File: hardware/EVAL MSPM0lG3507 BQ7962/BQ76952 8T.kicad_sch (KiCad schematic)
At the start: 54 parts, among them U11 FCX495, U13 PBQ76952PFBT, U14 FCX495

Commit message: kjcaejjacljace
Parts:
- added D3: D_Schottky_Small, symbol Device:D_Schottky_Small
- added R45: 200, Resistor_SMD:R_1206_3216Metric_Pad1.30x1.75mm_HandSolder, symbol Device:R_US
- added TP18: TestPoint, TestPoint:TestPoint_Loop_D2.50mm_Drill1.0mm_LowProfile, symbol Connector:TestPoint
- C36, C37, C38, C42, C43, C44, C45, C46, C47, C48, C49, C50, C51, C52, C53, C54, C55: mouser (none) -> https://www.mouser.com/ProductDetail/Samsung-Electro-Mechan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; specs (none) -> 50VDC, X7R, 10%, -55C, +125C, 220nF; unit x10 (none) -> 0.05
- C57: specs (none) -> 10uF, 50VDC, X5R, 10%, -55C, +85C; unit x10 (none) -> 0.07
- R72: mouser (none) -> https://www.mouser.com/ProductDetail/Panasonic/ERJ-P08J201V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; specs (none) -> 200Ohms, 660mW, 200PPM, 500V, 5%, -55C, +155C
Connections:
- net 16P: now also R45.2; no longer R65.2, U11.2
- net BAT: now also TP18.1
- new net: R45.1, R65.2, U11.2
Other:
- note added: "raise to 3.3v to shut off device"
- moved on the sheet: TP8

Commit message: mouser doom scrolling labor
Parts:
- removed C62: 1u, Capacitor_SMD:C_1812_4532Metric, symbol Device:C_Small
- removed D3: D_Schottky_Small, symbol Device:D_Schottky_Small
- removed R65: 50k, Resistor_SMD:R_1206_3216Metric_Pad1.30x1.75mm_HandSolder, symbol Device:R_US
- added C1, C2, C4, C6, C7: 10u, Capacitor_SMD:C_1206_3216Metric_Pad1.33x1.80mm_HandSolder, symbol Device:C_Small
- added D3: 36V, symbol Device:D_Zener_Small
- added R27, R46: 100k, Resistor_SMD:R_1206_3216Metric_Pad1.30x1.75mm_HandSolder, symbol Device:R_US
- C30, C56, C58, C59, C60, C61: mouser (none) -> https://www.mouser.com/ProductDetail/Walsin/1206B104K251CT?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; specs (none) -> 100nF, 250VDC, X7R, 10%, -55C, +125C; unit x10 (none) -> 0.062
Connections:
- net BAT: now also C1.1, C2.1, C4.1, C6.1
- net Series Sense N: now also C1.2, C2.2, C4.2, C6.2, C7.2, D3.2 (A)
- net at C56.1, U11.1: now also D3.1 (K), R46.1
- net at R45.1, U11.2: now also R27.2
- net at R72.2, U14.2: now also C7.1
- new net: R27.1, R46.2
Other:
- note added: "buffer caps. 434ms op @ 300mA from 6v src"
- note added: "power supply input pin (50V abs max, limited by caps)"
- moved on the sheet: C56

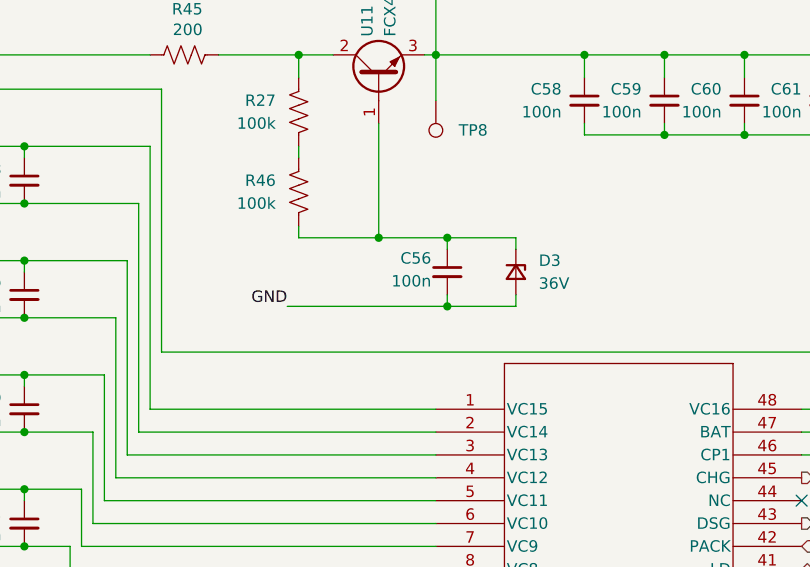
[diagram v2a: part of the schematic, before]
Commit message: ti once again making the most convenient IC's around
new TVS solution. use the
TPD4E05U06DQA
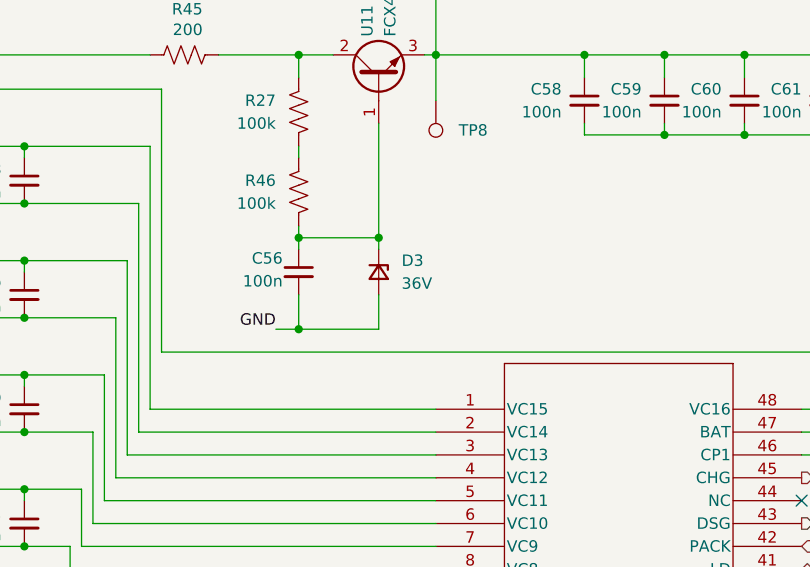
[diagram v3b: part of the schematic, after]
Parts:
- U11, U14: unit x10 (none) -> 0.34
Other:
- moved on the sheet: C56, D3
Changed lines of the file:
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@@
 	)
 	(junction
-		(at 135.89 54.61)
-		(diameter 0)
-		(color 0 0 0 0)
-	)
-	(junction
 		(at 176.53 43.18)
 		(diameter 0)
@@
 	)
 	(junction
+		(at 135.89 54.61)
+		(diameter 0)
+		(color 0 0 0 0)
+	)
+	(junction
 		(at 90.17 44.45)
 		(diameter 0)
@@
 	)
 	(junction
-		(at 90.17 95.25)
+		(at 127 64.77)
 		(diameter 0)
 		(color 0 0 0 0)
 	)
 	(junction
-		(at 143.51 62.23)
+		(at 90.17 95.25)
 		(diameter 0)
 		(color 0 0 0 0)
@@
 	)
 	(junction
+		(at 127 54.61)
+		(diameter 0)
+		(color 0 0 0 0)
+	)
+	(junction
 		(at 96.52 44.45)
 		(diameter 0)
@@
 	)
 	(junction
-		(at 143.51 54.61)
-		(diameter 0)
-		(color 0 0 0 0)
-	)
-	(junction
 		(at 190.5 52.07)
 		(diameter 0)
@@
 	(wire
 		(pts
-			(xy 143.51 60.96) (xy 143.51 62.23)
-		)
-		(stroke
-			(width 0)
-			(type default)
-		)
-	)
-	(wire
-		(pts
 			(xy 53.34 44.45) (xy 72.39 44.45)
 		)
@@
 	(wire
 		(pts
-			(xy 135.89 54.61) (xy 143.51 54.61)
-		)
-		(stroke
-			(width 0)
-			(type default)
-		)
-	)
-	(wire
-		(pts
 			(xy 90.17 57.15) (xy 96.52 57.15)
 		)
@@
 	(wire
 		(pts
+			(xy 127 60.96) (xy 127 64.77)
+		)
+		(stroke
+			(width 0)
+			(type default)
+		)
+	)
+	(wire
+		(pts
 			(xy 90.17 107.95) (xy 96.52 107.95)
 		)
@@
 	(wire
 		(pts
+			(xy 127 54.61) (xy 135.89 54.61)
+		)
+		(stroke
+			(width 0)
+			(type default)
+		)
+	)
+	(wire
+		(pts
 			(xy 90.17 128.27) (xy 90.17 127)
 		)
@@
 	(wire
 		(pts
-			(xy 151.13 62.23) (xy 151.13 60.96)
+			(xy 135.89 64.77) (xy 135.89 60.96)
 		)
 		(stroke
@@
 	(wire
 		(pts
-			(xy 151.13 62.23) (xy 143.51 62.23)
+			(xy 135.89 64.77) (xy 127 64.77)
 		)
 		(stroke
@@
 	(wire
 		(pts
-			(xy 127 54.61) (xy 135.89 54.61)
-		)
-		(stroke
-			(width 0)
-			(type default)
-		)
-	)
-	(wire
-		(pts
 			(xy 138.43 132.08) (xy 138.43 134.62)
 		)
@@
 	(wire
 		(pts
-			(xy 143.51 55.88) (xy 143.51 54.61)
+			(xy 127 55.88) (xy 127 54.61)
 		)
 		(stroke
@@
 	(wire
 		(pts
-			(xy 151.13 54.61) (xy 143.51 54.61)
-		)
-		(stroke
-			(width 0)
-			(type default)
-		)
-	)
-	(wire
-		(pts
 			(xy 46.99 72.39) (xy 52.07 72.39)
 		)
@@
 	(wire
 		(pts
-			(xy 151.13 54.61) (xy 151.13 55.88)
+			(xy 135.89 54.61) (xy 135.89 55.88)
 		)
 		(stroke
@@
 	(wire
 		(pts
-			(xy 125.73 62.23) (xy 143.51 62.23)
+			(xy 124.46 64.77) (xy 127 64.77)
 		)
 		(stroke
@@
 	)
 	(label "GND"
-		(at 125.73 62.23 180)
+		(at 124.46 64.77 180)
 		(effects
 			(font
@@
 			)
 		)
+		(property "unit x10" "0.34"
+			(at 135.89 35.56 0)
+			(effects
+				(font
+					(size 1.27 1.27)
+				)
+				(hide yes)
+			)
+		)
 		(pin "1"
 		)
@@
 	)
 	(symbol
-		(lib_name "FCX485_NPN_BJT_1")
 		(lib_id "zzLocalLibrary:FCX485_NPN_BJT")
 		(at 207.01 95.25 0)
@@
 			)
 		)
+		(property "unit x10" "0.34"
+			(at 207.01 95.25 0)
+			(effects
+				(font
+					(size 1.27 1.27)
+				)
+				(hide yes)
+			)
+		)
 		(pin "1"
 		)
@@
 	(symbol
 		(lib_id "Device:C_Small")
-		(at 143.51 58.42 0)
+		(at 127 58.42 0)
 		(mirror y)
 		(unit 1)
@@
 		(dnp no)
 		(property "Reference" "C56"
-			(at 141.732 56.896 0)
+			(at 125.222 56.896 0)
 			(effects
 				(font
@@
 		)
 		(property "Value" "100n"
-			(at 141.732 59.436 0)
+			(at 125.222 59.436 0)
 			(effects
 				(font
@@
 		)
 		(property "Footprint" "Capacitor_SMD:C_1206_3216Metric_Pad1.33x1.80mm_HandSolder"
-			(at 143.51 58.42 0)
+			(at 127 58.42 0)
 			(effects
 				(font
@@
 		)
 		(property "Datasheet" ""
-			(at 143.51 58.42 0)
+			(at 127 58.42 0)
 			(effects
 				(font
@@
 		)
 		(property "Description" ""
-			(at 143.51 58.42 0)
+			(at 127 58.42 0)
 			(effects
 				(font
@@
 		)
 		(property "Sim.Device" ""
-			(at 143.51 58.42 0)
+			(at 127 58.42 0)
 			(effects
 				(font
@@
 		)
 		(property "Sim.Type" ""
-			(at 143.51 58.42 0)
+			(at 127 58.42 0)
 			(effects
 				(font
@@
 		)
 		(property "mouser" "https://www.mouser.com/ProductDetail/Walsin/1206B104K251CT?qs=fIkAfuXiAQKkmX5niKUTKw%3D%3D"
-			(at 143.51 58.42 0)
+			(at 127 58.42 0)
 			(effects
 				(font
@@
 		)
 		(property "specs" "100nF, 250VDC, X7R, 10%, -55C, +125C"
-			(at 143.51 58.42 0)
+			(at 127 58.42 0)
 			(effects
 				(font
@@
 		)
 		(property "unit x10" "0.062"
-			(at 143.51 58.42 0)
+			(at 127 58.42 0)
 			(effects
 				(font
@@
 	(symbol
 		(lib_id "Device:D_Zener_Small")
-		(at 151.13 58.42 270)
+		(at 135.89 58.42 270)
 		(unit 1)
 		(exclude_from_sim no)
@@
 		(fields_autoplaced yes)
 		(property "Reference" "D3"
-			(at 153.67 57.1499 90)
+			(at 138.43 57.1499 90)
 			(effects
 				(font
@@
 		)
 		(property "Value" "36V"
-			(at 153.67 59.6899 90)
+			(at 138.43 59.6899 90)
 			(effects
 				(font
@@
 		)
 		(property "Footprint" ""
-			(at 151.13 58.42 90)
+			(at 135.89 58.42 90)
 			(effects
 				(font
@@
 		)
 		(property "Datasheet" "~"
-			(at 151.13 58.42 90)
+			(at 135.89 58.42 90)
 			(effects
 				(font
@@
 		)
 		(property "Description" "Zener diode, small symbol"
-			(at 151.13 58.42 0)
+			(at 135.89 58.42 0)
 			(effects
 				(font
@@
 		)
 		(property "mouser" "https://www.mouser.com/ProductDetail/Vishay/MMSZ4715-HE3_A-08?qs=Imq1NPwxi74N8IHyuuRB%252BQ%3D%3D"
-			(at 151.13 58.42 0)
+			(at 135.89 58.42 0)
 			(effects
 				(font
@@
 		)
 		(property "specs" "36V, 500mW, 5%, 1nA, -55C, +150C"
-			(at 151.13 58.42 0)
+			(at 135.89 58.42 0)
 			(effects
 				(font
@@
 		)
 		(property "unit x10" "0.27"
-			(at 151.13 58.42 0)
+			(at 135.89 58.42 0)
 			(effects
 				(font

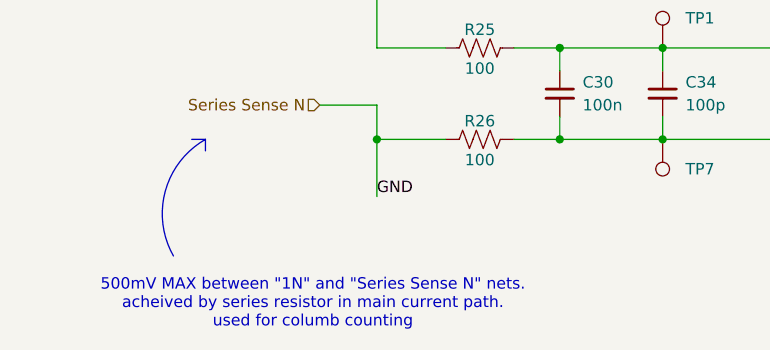
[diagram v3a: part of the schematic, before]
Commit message: corrected mosfet choice and started jumper board with xds110
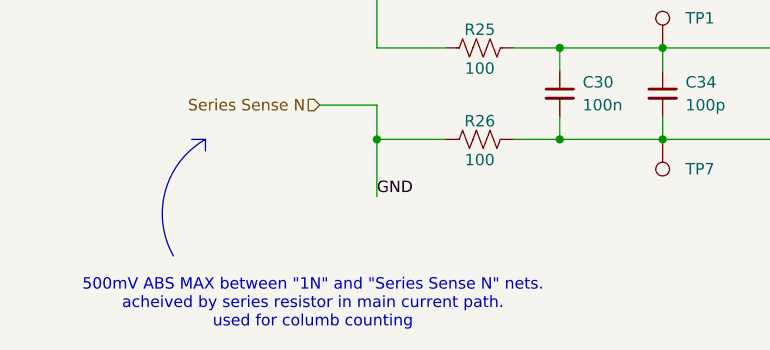
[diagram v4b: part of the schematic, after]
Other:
- note added: "500mV ABS MAX between "1N" and "Series Sense N" nets. acheived by series resistor in main current path. used for columb counting"
- note removed: "500mV MAX between "1N" and "Series Sense N" nets. acheived by series resistor in main current path. used for columb counting"
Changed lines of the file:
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@@
 		)
 	)
-	(text "500mV MAX between \"1N\" and \"Series Sense N\" nets.\nacheived by series resistor in main current path.\nused for columb counting"
+	(text "500mV ABS MAX between \"1N\" and \"Series Sense N\" nets.\nacheived by series resistor in main current path.\nused for columb counting"
 		(exclude_from_sim no)
 		(at 46.228 191.008 0)

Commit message: indicated layout so someone else can do it
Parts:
- D3: footprint (none) -> Diode_SMD:D_SOD-123
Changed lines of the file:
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@@
 			)
 		)
-		(property "Footprint" ""
+		(property "Footprint" "Diode_SMD:D_SOD-123"
 			(at 135.89 58.42 90)
 			(effects

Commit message: complete layout
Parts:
- removed TP8: TestPoint, TestPoint:TestPoint_Loop_D2.50mm_Drill1.0mm_LowProfile, symbol Connector:TestPoint
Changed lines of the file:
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@@
 	(wire
 		(pts
-			(xy 142.24 34.29) (xy 142.24 39.37)
-		)
-		(stroke
-			(width 0)
-			(type default)
-		)
-	)
-	(wire
-		(pts
 			(xy 90.17 50.8) (xy 96.52 50.8)
 		)
@@
 		(pin "1"
 		)
-		(instances
-			(project ""
-				(path "/20ac6af0-79b5-4ba6-aad3-75081d02c913/ba45ce94-ada4-466b-9390-9916681e599d"
-					(reference "D3")
-					(unit 1)
-				)
-			)
-		)
 	)
 	(symbol
@@
 					(unit 1)
 				)
-			)
-		)
-	)
-	(symbol
-		(lib_id "Connector:TestPoint")
-		(at 142.24 39.37 180)
-		(unit 1)
-		(exclude_from_sim no)
-		(in_bom no)
-		(on_board yes)
-		(dnp no)
-		(fields_autoplaced yes)
-		(property "Reference" "TP8"
-			(at 144.78 42.6719 0)
-			(effects
-				(font
-					(size 1.27 1.27)
-				)
-				(justify right)
-			)
-		)
-		(property "Value" "TestPoint"
-			(at 139.7 41.4021 0)
-			(effects
-				(font
-					(size 1.27 1.27)
-				)
-				(justify left)
-				(hide yes)
-			)
-		)
-		(property "Footprint" "TestPoint:TestPoint_Loop_D2.50mm_Drill1.0mm_LowProfile"
-			(at 137.16 39.37 0)
-			(effects
-				(font
-					(size 1.27 1.27)
-				)
-				(hide yes)
-			)
-		)
-		(property "Datasheet" "~"
-			(at 137.16 39.37 0)
-			(effects
-				(font
-					(size 1.27 1.27)
-				)
-				(hide yes)
-			)
-		)
-		(property "Description" "test point"
-			(at 142.24 39.37 0)
-			(effects
-				(font
-					(size 1.27 1.27)
-				)
-				(hide yes)
-			)
-		)
-		(property "Sim.Device" ""
-			(at 142.24 39.37 90)
-			(effects
-				(font
-					(size 1.27 1.27)
-				)
-				(hide yes)
-			)
-		)
-		(property "Sim.Type" ""
-			(at 142.24 39.37 90)
-			(effects
-				(font
-					(size 1.27 1.27)
-				)
-				(hide yes)
-			)
-		)
-		(pin "1"
-		)
-		(instances
-			(project "EVAL MSPM0lG3507 BQ7962"
-				(path "/20ac6af0-79b5-4ba6-aad3-75081d02c913/ba45ce94-ada4-466b-9390-9916681e599d"
-					(reference "TP8")
-					(unit 1)
-				)
